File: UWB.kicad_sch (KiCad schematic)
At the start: 0 parts

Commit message: UWB: DWM3000 schematic with decoupling, IRQ pulldown and status LEDs
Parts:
- added D1, D2: LED, LED_SMD:LED_Cree-XHP50_3V_HighDensity, symbol Device:LED
- added R1: 100k, lcsc_footprints:C5299931_WIRELM-SMD_DWM3000TR13, symbol Device:R
- added U1: DWM3000TR13, lcsc_footprints:C5299931_WIRELM-SMD_DWM3000TR13, symbol lcsc_imported:DWM3000TR13
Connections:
- new net: D1.2 (A), U1.12 (GPIO3)
- new net: D2.2 (A), U1.13 (GPIO2)
- new net: R1.1, U1.22 (GPIO8)
- new net +3.3V: U1.5 (VDD1), U1.6 (VDD3V3), U1.7 (VDD3V3)
- new net DWM3000_RSTn: U1.3 (RSTn)
- new net GND: R1.2, U1.16 (VSS), U1.21 (VSS), U1.23 (VSS), U1.24 (VSS), U1.8 (VSS)
- no-connect marks 0 -> 2

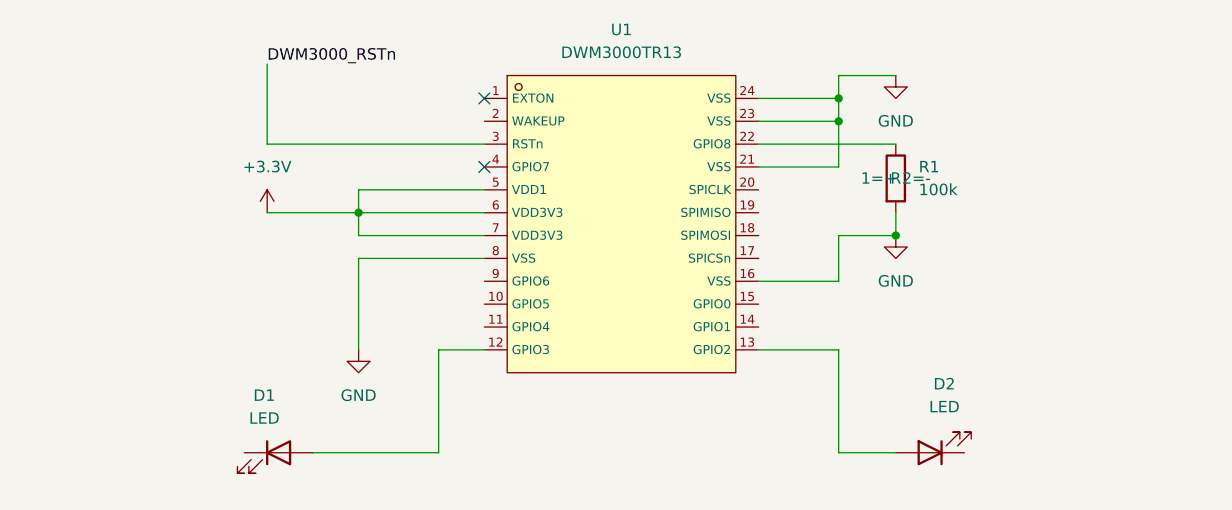
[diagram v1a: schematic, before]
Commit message: UWB: restore full schematic (decoupling, LED resistors, IRQ pulldown, hierarchical labels)
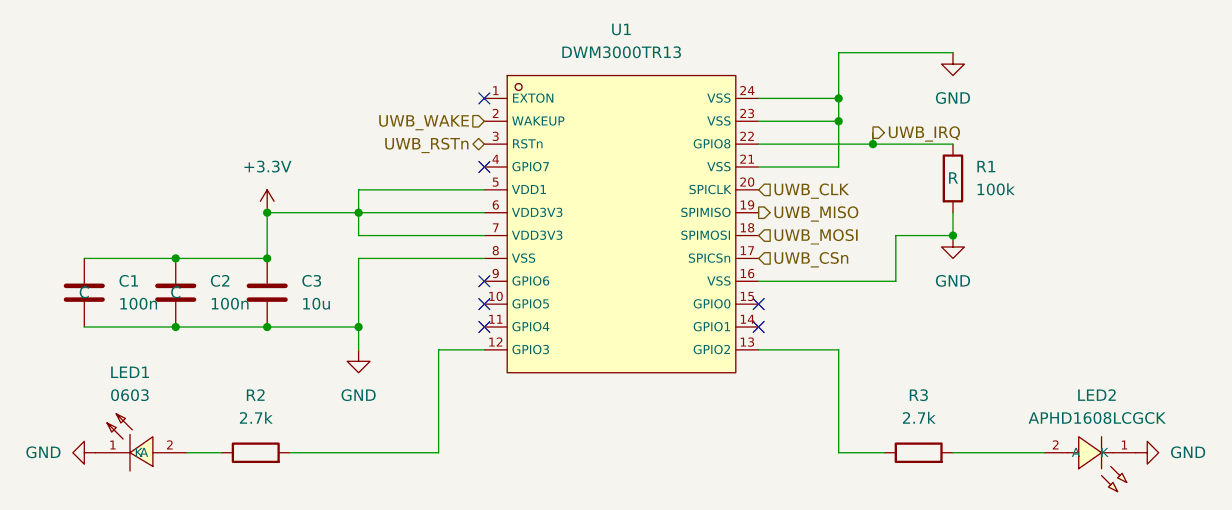
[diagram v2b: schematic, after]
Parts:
- removed D1, D2: LED, LED_SMD:LED_Cree-XHP50_3V_HighDensity, symbol Device:LED
- added C1, C2: 100n, symbol Device:C
- added C3: 10u, symbol Device:C
- added LED1: 0603, lcsc_footprints:C2289_LED0603-RD, symbol lcsc_imported:0603
- added LED2: APHD1608LCGCK, lcsc_footprints:C5139863_LED-SMD_L1_6-W0_8-RD_GREEN-1, symbol lcsc_imported:APHD1608LCGCK
- added R2, R3: 2.7k, lcsc_footprints:C5139863_LED-SMD_L1_6-W0_8-RD_GREEN-1, symbol Device:R
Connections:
- net +3.3V: now also C1.1, C2.1, C3.1
- net GND: now also C1.2, C2.2, C3.2, LED1.1 (K), LED2.1 (K)
- net at U1.12 (GPIO3): now also R2.2
- net at U1.13 (GPIO2): now also R3.1
- net UWB_CSn: now reaches U1.17 (SPICSn)
- net UWB_MOSI: now reaches U1.18 (SPIMOSI)
- net UWB_MISO: now reaches U1.19 (SPIMISO)
- net UWB_WAKE: now reaches U1.2 (WAKEUP)
- net UWB_CLK: now reaches U1.20 (SPICLK)
- net UWB_IRQ: now reaches R1.1, U1.22 (GPIO8)
- net DWM3000_RSTn renamed UWB_RSTn
- new net: LED1.2 (A), R2.1
- new net: LED2.2 (A), R3.2
- no-connect marks 2 -> 7
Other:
- moved on the sheet: R1
